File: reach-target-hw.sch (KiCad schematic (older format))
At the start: 0 parts

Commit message: "qfaa qfn48 w/ dcdc" reference design in
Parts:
- added AE?: ANTENNA, symbol ANTENNA
- added C1, C13, C14, C2: 12pF, symbol C
- added C10: 47nF, symbol C
- added C11, C8: 100nF, symbol C
- added C12: 1.0uF, symbol C
- added C3: 2.2nF, symbol C
- added C4: 1pF, symbol C
- added C5: 2.2pF, symbol C
- added C6: 1.5pF, symbol C
- added C7: 4.7uF, symbol C
- added C9: 1nF, symbol C
- added L1: 4.7nH, symbol INDUCTOR
- added L2: 10nH, symbol INDUCTOR
- added L3: 3.3nH, symbol INDUCTOR
- added L4: 10uH, symbol INDUCTOR
- added L5: 15nH, symbol INDUCTOR
- added U1: nRF51822-QF, symbol nRF51822-QF
- added X1: 16MHz, symbol CRYSTAL
- added X2: 32.768kHz, symbol CRYSTAL
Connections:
- net labels added: +3V3, AVDD_NRF, DCC, DCC-I, DEC1, DEC2, GND, SWDCLK, SWDIO/~RESET, XC1, XC2, XL1, XL2
- wire segments 0 -> 65
- no-connect marks 0 -> 1

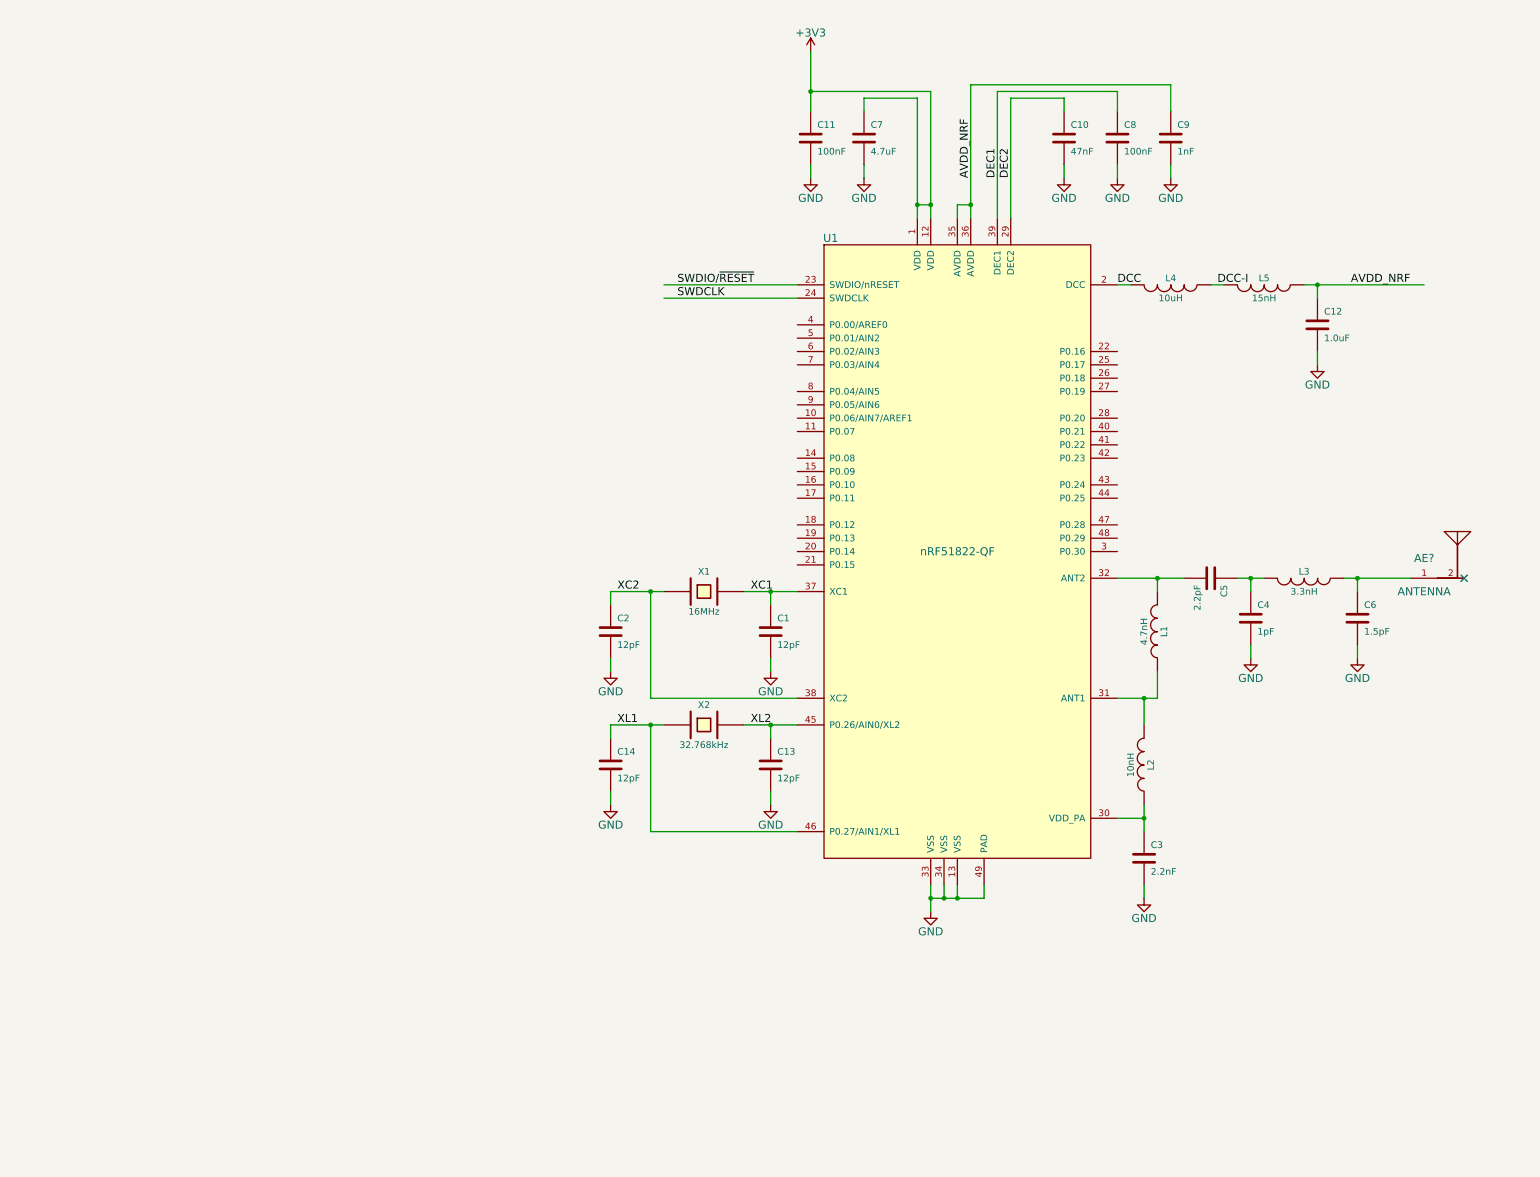
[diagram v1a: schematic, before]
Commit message: more precise values, packages
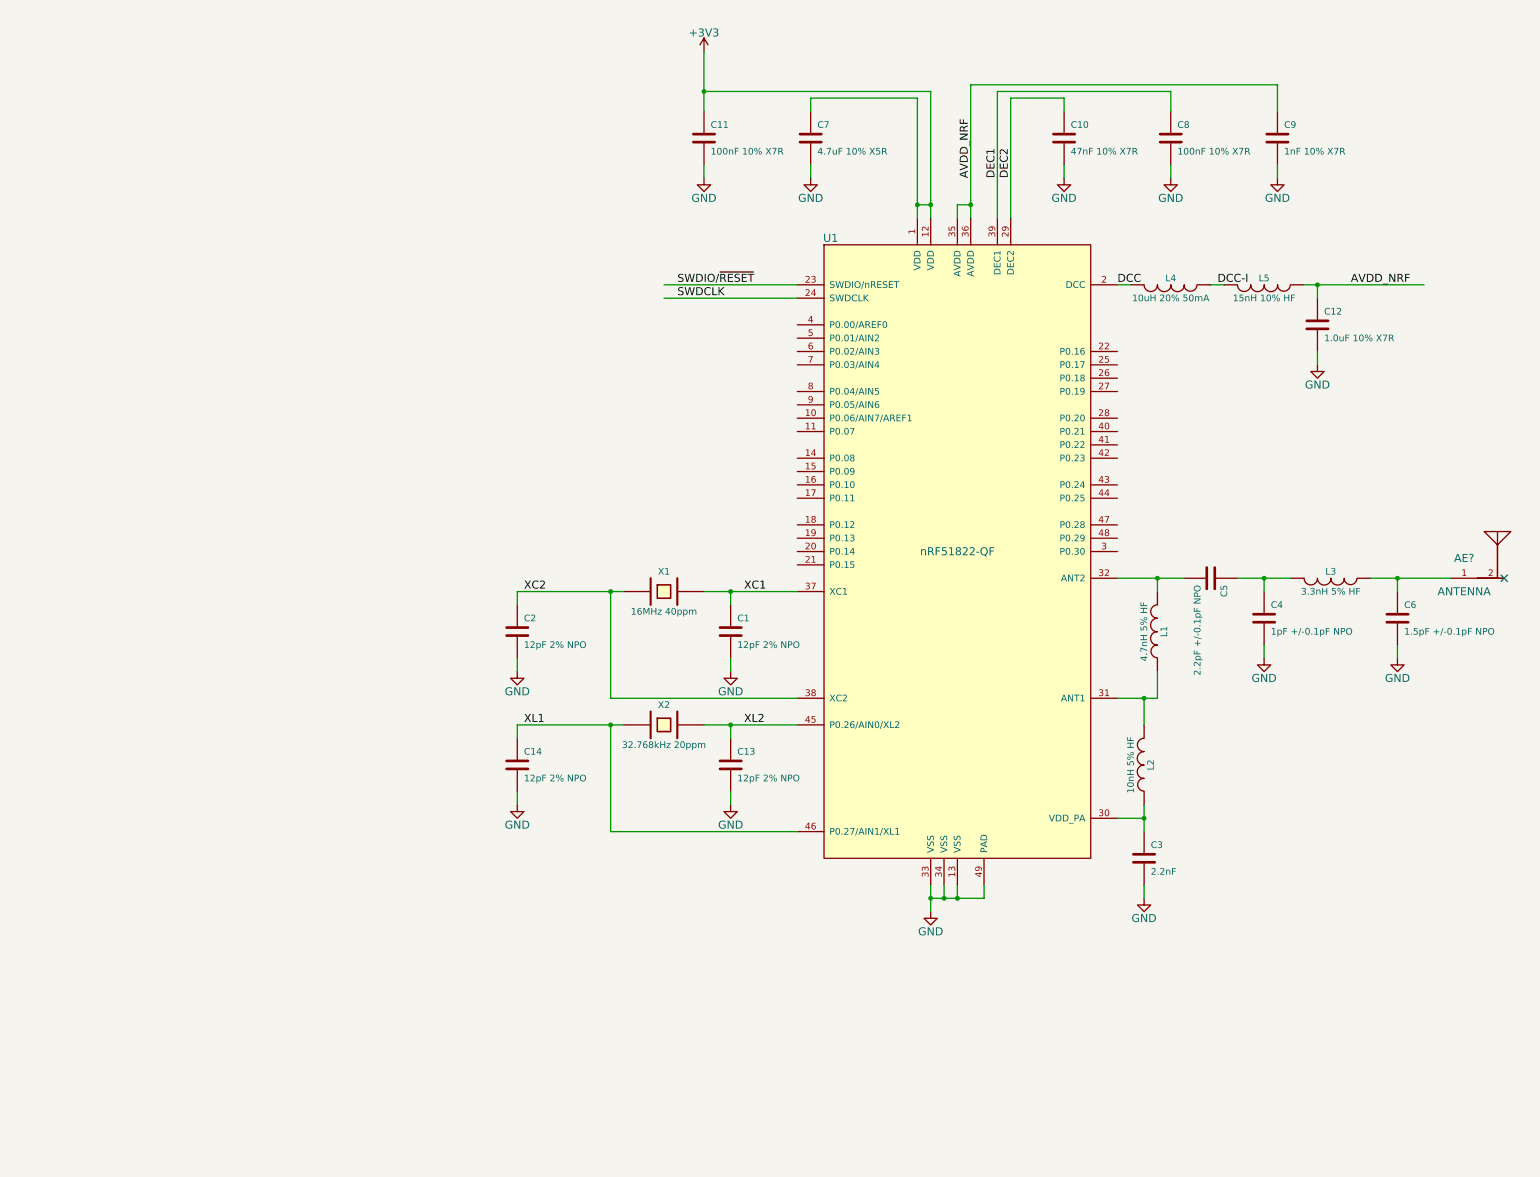
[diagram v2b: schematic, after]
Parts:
- C1, C13, C14, C2: value 12pF -> 12pF 2% NPO
- C10: value 47nF -> 47nF 10% X7R
- C11, C8: value 100nF -> 100nF 10% X7R
- C12: value 1.0uF -> 1.0uF 10% X7R; footprint (none) -> !Parts:SMD-0603
- C4: value 1pF -> 1pF +/-0.1pF NPO
- C5: value 2.2pF -> 2.2pF +/-0.1pF NPO
- C6: value 1.5pF -> 1.5pF +/-0.1pF NPO
- C7: value 4.7uF -> 4.7uF 10% X5R; footprint (none) -> !Parts:SMD-0603
- C9: value 1nF -> 1nF 10% X7R
- L1: value 4.7nH -> 4.7nH 5% HF
- L2: value 10nH -> 10nH 5% HF
- L3: value 3.3nH -> 3.3nH 5% HF
- L4: value 10uH -> 10uH 20% 50mA; footprint (none) -> !Parts:SMD-0603
- L5: value 15nH -> 15nH 10% HF
- X1: value 16MHz -> 16MHz 40ppm
- X2: value 32.768kHz -> 32.768kHz 20ppm
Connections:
- wire segments 65 -> 82
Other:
- moved on the sheet: AE?, C1, C11, C13, C14, C2, C4, C6, C7, C8, C9, L3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

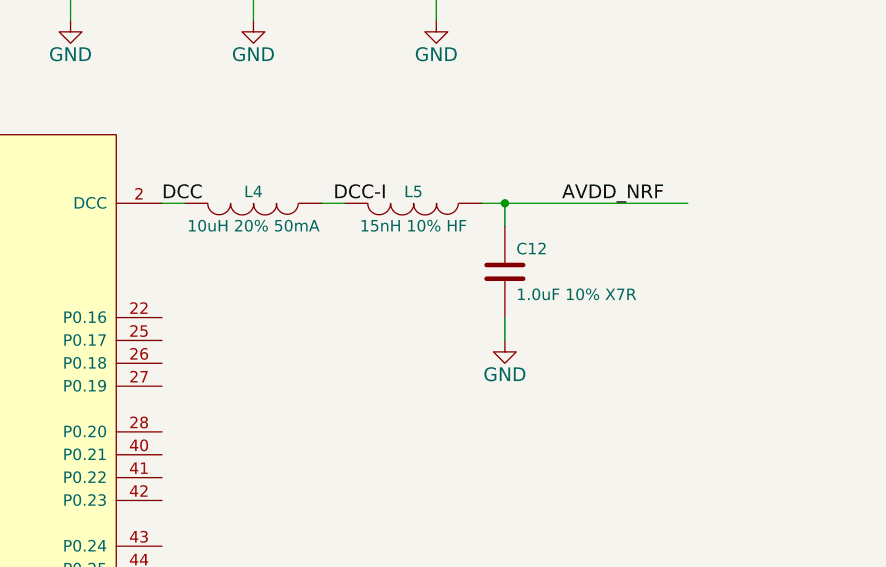
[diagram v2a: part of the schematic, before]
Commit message: underscores over hyphens
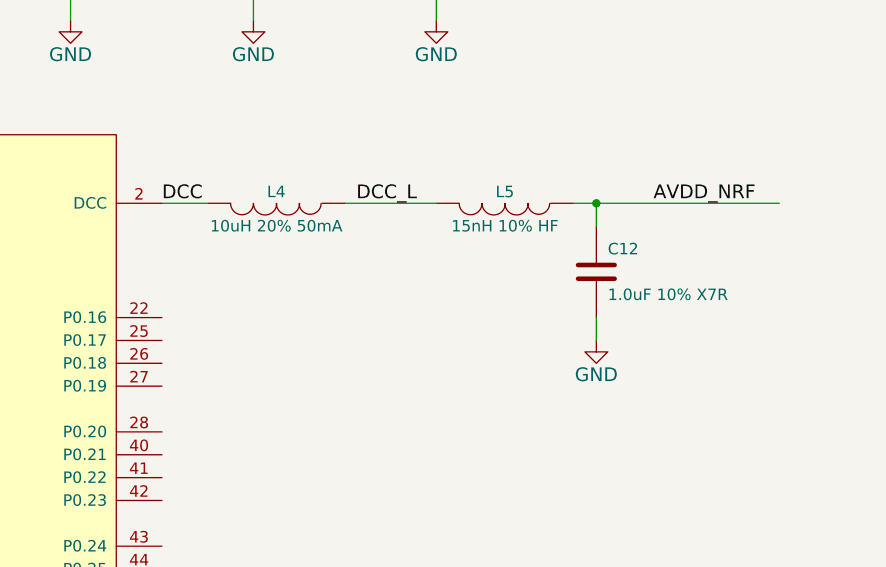
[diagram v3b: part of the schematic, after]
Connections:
- net labels added: DCC_L
- net labels removed: DCC-I
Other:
- moved on the sheet: C12, L4, L5
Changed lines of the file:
@@
 L INDUCTOR L4
 U 1 1 54D11F7B
-P 10000 3400
-F 0 "L4" V 9950 3400 50  0000 C CNN
-F 1 "10uH 20% 50mA" V 10100 3400 50  0000 C CNN
-F 2 "!Parts:SMD-0603" H 10000 3400 60  0001 C CNN
-F 3 "" H 10000 3400 60  0000 C CNN
-	1    10000 3400
+P 10100 3400
+F 0 "L4" V 10050 3400 50  0000 C CNN
+F 1 "10uH 20% 50mA" V 10200 3400 50  0000 C CNN
+F 2 "!Parts:SMD-0603" H 10100 3400 60  0001 C CNN
+F 3 "" H 10100 3400 60  0000 C CNN
+	1    10100 3400
 	0    1    1    0
 $EndComp
@@
 L INDUCTOR L5
 U 1 1 54D128EE
-P 10700 3400
-F 0 "L5" V 10650 3400 50  0000 C CNN
-F 1 "15nH 10% HF" V 10800 3400 50  0000 C CNN
-F 2 "" H 10700 3400 60  0000 C CNN
-F 3 "" H 10700 3400 60  0000 C CNN
-	1    10700 3400
+P 11100 3400
+F 0 "L5" V 11050 3400 50  0000 C CNN
+F 1 "15nH 10% HF" V 11200 3400 50  0000 C CNN
+F 2 "" H 11100 3400 60  0000 C CNN
+F 3 "" H 11100 3400 60  0000 C CNN
+	1    11100 3400
 	0    1    1    0
 $EndComp
@@
 L C C12
 U 1 1 54D12946
-P 11100 3700
-F 0 "C12" H 11150 3800 50  0000 L CNN
-F 1 "1.0uF 10% X7R" H 11150 3600 50  0000 L CNN
-F 2 "!Parts:SMD-0603" H 11138 3550 30  0001 C CNN
-F 3 "" H 11100 3700 60  0000 C CNN
-	1    11100 3700
+P 11500 3700
+F 0 "C12" H 11550 3800 50  0000 L CNN
+F 1 "1.0uF 10% X7R" H 11550 3600 50  0000 L CNN
+F 2 "!Parts:SMD-0603" H 11538 3550 30  0001 C CNN
+F 3 "" H 11500 3700 60  0000 C CNN
+	1    11500 3700
 	1    0    0    -1
 $EndComp
@@
 L GND #PWR?
 U 1 1 54D1536C
-P 11100 4000
-F 0 "#PWR?" H 11100 3750 60  0001 C CNN
-F 1 "GND" H 11100 3850 60  0000 C CNN
-F 2 "" H 11100 4000 60  0000 C CNN
-F 3 "" H 11100 4000 60  0000 C CNN
-	1    11100 4000
+P 11500 4000
+F 0 "#PWR?" H 11500 3750 60  0001 C CNN
+F 1 "GND" H 11500 3850 60  0000 C CNN
+F 2 "" H 11500 4000 60  0000 C CNN
+F 3 "" H 11500 4000 60  0000 C CNN
+	1    11500 4000
 	1    0    0    -1
 $EndComp
@@
 Text Label 9600 3400 0    60   ~ 0
 DCC
-Text Label 10350 3400 0    60   ~ 0
-DCC-I
-Text Label 11350 3400 0    60   ~ 0
+Text Label 10450 3400 0    60   ~ 0
+DCC_L
+Text Label 11750 3400 0    60   ~ 0
 AVDD_NRF
 $Comp
@@
 	5100 7300 5100 7200
 Wire Wire Line
-	9600 3400 9700 3400
-Wire Wire Line
-	10300 3400 10400 3400
-Wire Wire Line
-	11000 3400 11100 3400
-Wire Wire Line
-	11100 3400 11900 3400
-Wire Wire Line
-	11100 3400 11100 3500
-Wire Wire Line
-	11100 4000 11100 3900
-Connection ~ 11100 3400
+	9600 3400 9800 3400
+Wire Wire Line
+	10400 3400 10800 3400
+Wire Wire Line
+	11400 3400 11500 3400
+Wire Wire Line
+	11500 3400 12300 3400
+Wire Wire Line
+	11500 3400 11500 3500
+Wire Wire Line
+	11500 4000 11500 3900
+Connection ~ 11500 3400
 Wire Wire Line
 	8800 2900 8800 2000

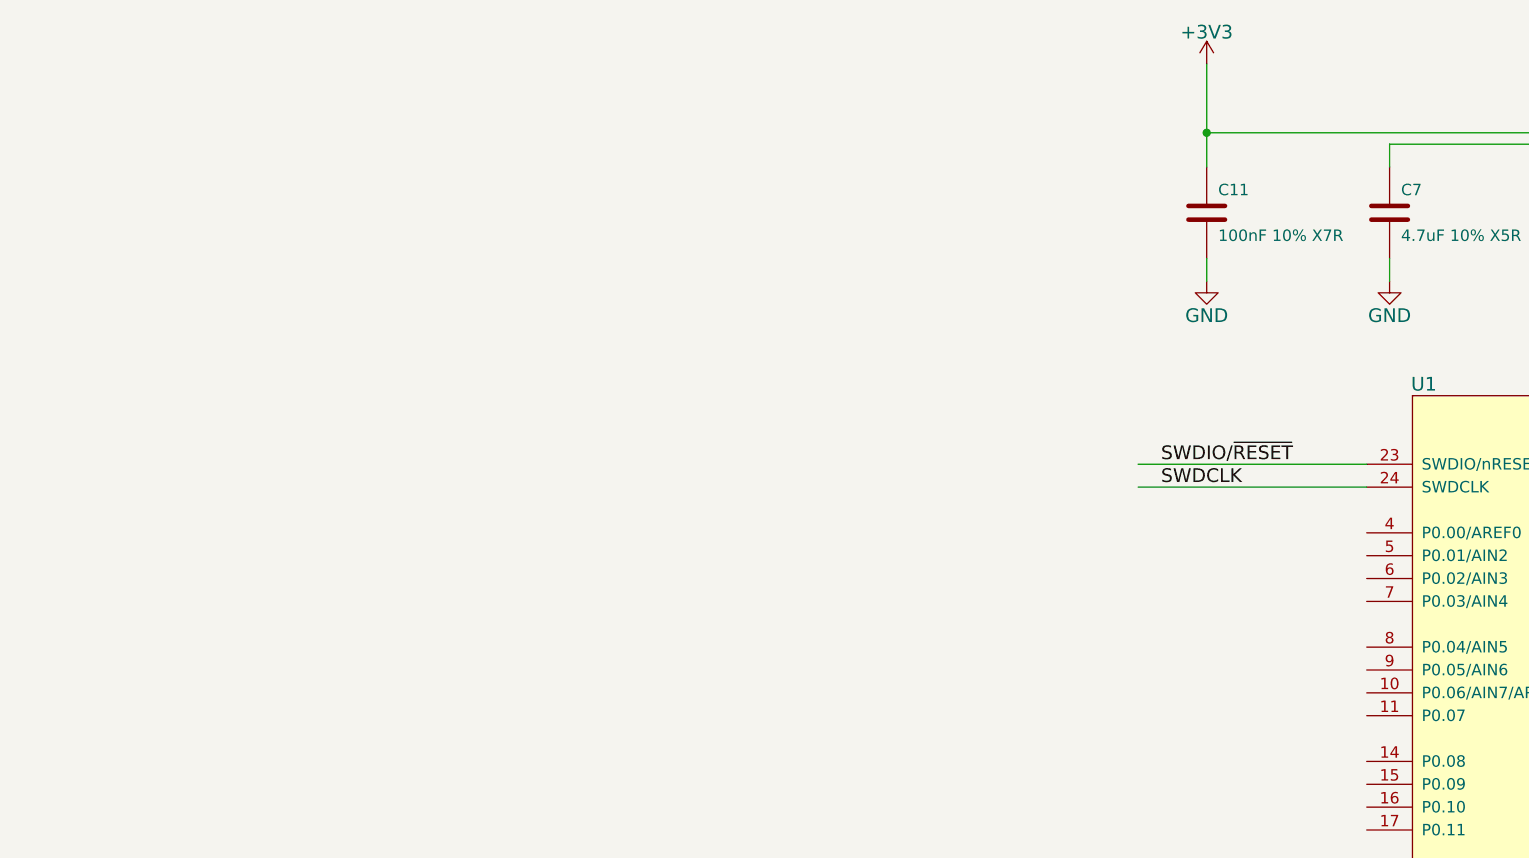
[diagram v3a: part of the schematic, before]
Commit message: added power plant (ncp103). still needs some tweaks re. enable line...
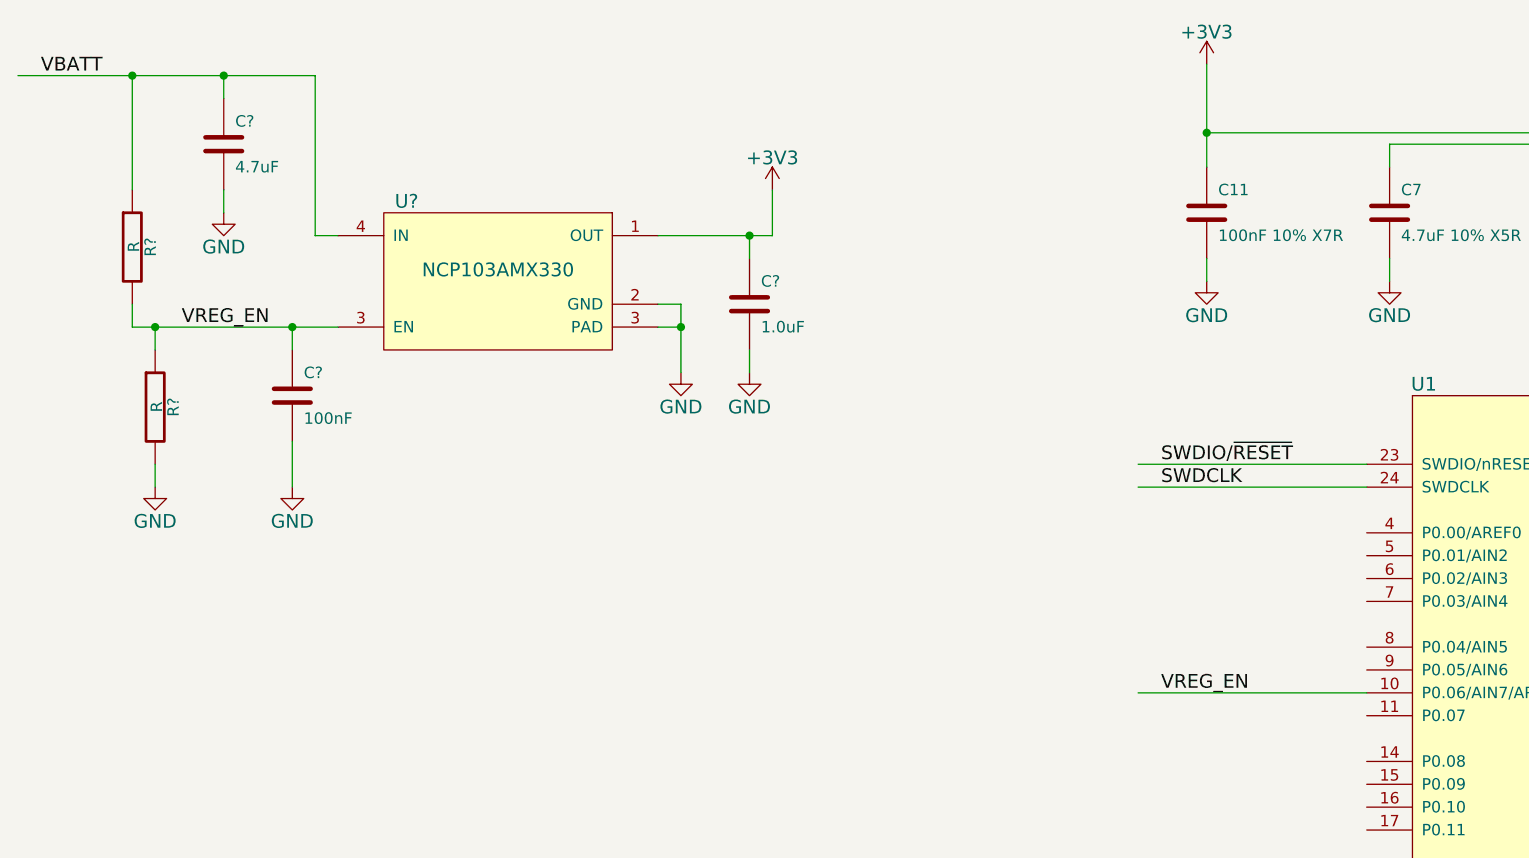
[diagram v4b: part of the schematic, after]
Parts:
- added C?: 4.7uF, !Parts:SMD-0603, symbol C
- added C?: 1.0uF, !Parts:SMD-0603, symbol C
- added C?: 100nF, !Parts:SMD-0603, symbol C
- added R? (x2): R, symbol R
- added U?: NCP103AMX330, tm-kicad-lib:UDFN4_1EP, symbol NCP103
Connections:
- net labels added: VBATT, VREG_EN
- wire segments 82 -> 108
